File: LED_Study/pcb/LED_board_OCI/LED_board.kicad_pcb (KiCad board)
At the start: 2 copper layers, 25.4 x 25.4 mm, 4 parts

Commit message: new boards
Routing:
- net /Vin: track 10.5 -> 0.00 mm
- net /GND: track 10.5 -> 0.00 mm
- net Net-(D3-Pad1): track 9.07 -> 0.00 mm
- net Net-(D1-Pad1): track 9.07 -> 0.00 mm
- added copper zone on F.Cu, net /GND
- added copper zone on F.Cu, net /Vin
- added copper zone on F.Cu, net Net-(D1-Pad1)
- added copper zone on F.Cu, net Net-(D3-Pad1)
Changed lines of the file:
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@@
   (gr_circle (center 100 100) (end 112.7 100)
     (stroke (width 0.1) (type default)) (fill none) (layer "Edge.Cuts"))
-  (segment (start 94.436 92) (end 92 94.436) (width 1) (layer "F.Cu") (net 1))
-  (segment (start 92 94.436) (end 92 97.25) (width 1) (layer "F.Cu") (net 1))
-  (segment (start 97.25 92) (end 94.436 92) (width 1) (layer "F.Cu") (net 1))
-  (segment (start 92 108) (end 97.25 108) (width 1) (layer "F.Cu") (net 3))
-  (segment (start 92 108) (end 92 102.75) (width 1) (layer "F.Cu") (net 3))
   (via (at 92 108) (size 3) (drill 1.5) (layers "F.Cu" "B.Cu") (free) (net 3))
-  (segment (start 108 92) (end 102.75 92) (width 1) (layer "F.Cu") (net 4))
-  (segment (start 108 92) (end 108 97.25) (width 1) (layer "F.Cu") (net 4))
   (via (at 108 92) (size 3) (drill 1.5) (layers "F.Cu" "B.Cu") (free) (net 4))
-  (segment (start 105.684 108.204) (end 108.12 105.768) (width 1) (layer "F.Cu") (net 6))
-  (segment (start 108.12 105.768) (end 108.12 102.954) (width 1) (layer "F.Cu") (net 6))
-  (segment (start 102.87 108.204) (end 105.684 108.204) (width 1) (layer "F.Cu") (net 6))
+  (zone (net 3) (net_name "/Vin") (layer "F.Cu") (hatch edge 0.5)
+    (priority 1)
+    (connect_pads (clearance 0.5))
+    (min_thickness 0.25) (filled_areas_thickness no)
+    (fill yes (thermal_gap 0.5) (thermal_bridge_width 0.5))
+    (polygon
+      (pts
+        (xy 100 100)
+        (xy 100 114)
+        (xy 86 114)
+        (xy 86 100)
+      )
+    )
+  )
+  (zone (net 4) (net_name "/GND") (layer "F.Cu") (hatch edge 0.5)
+    (priority 3)
+    (connect_pads (clearance 0.5))
+    (min_thickness 0.25) (filled_areas_thickness no)
+    (fill yes (thermal_gap 0.5) (thermal_bridge_width 0.5))
+    (polygon
+      (pts
+        (xy 100 100)
+        (xy 100 86)
+        (xy 113.5 86)
+        (xy 113.5 100)
+      )
+    )
+  )
+  (zone (net 6) (net_name "Net-(D3-Pad1)") (layer "F.Cu") (hatch edge 0.5)
+    (priority 2)
+    (connect_pads (clearance 0.5))
+    (min_thickness 0.25) (filled_areas_thickness no)
+    (fill yes (thermal_gap 0.5) (thermal_bridge_width 0.5))
+    (polygon
+      (pts
+        (xy 100 100)
+        (xy 113.5 100)
+        (xy 113.5 114)
+        (xy 100 114)
+      )
+    )
+  )
+  (zone (net 1) (net_name "Net-(D1-Pad1)") (layer "F.Cu") (hatch edge 0.5)
+    (priority 1)
+    (connect_pads (clearance 0.5))
+    (min_thickness 0.25) (filled_areas_thickness no)
+    (fill yes (thermal_gap 0.5) (thermal_bridge_width 0.5))
+    (polygon
+      (pts
+        (xy 100 100)
+        (xy 100 86)
+        (xy 86 86)
+        (xy 86 100)
+      )
+    )
+  )
 )

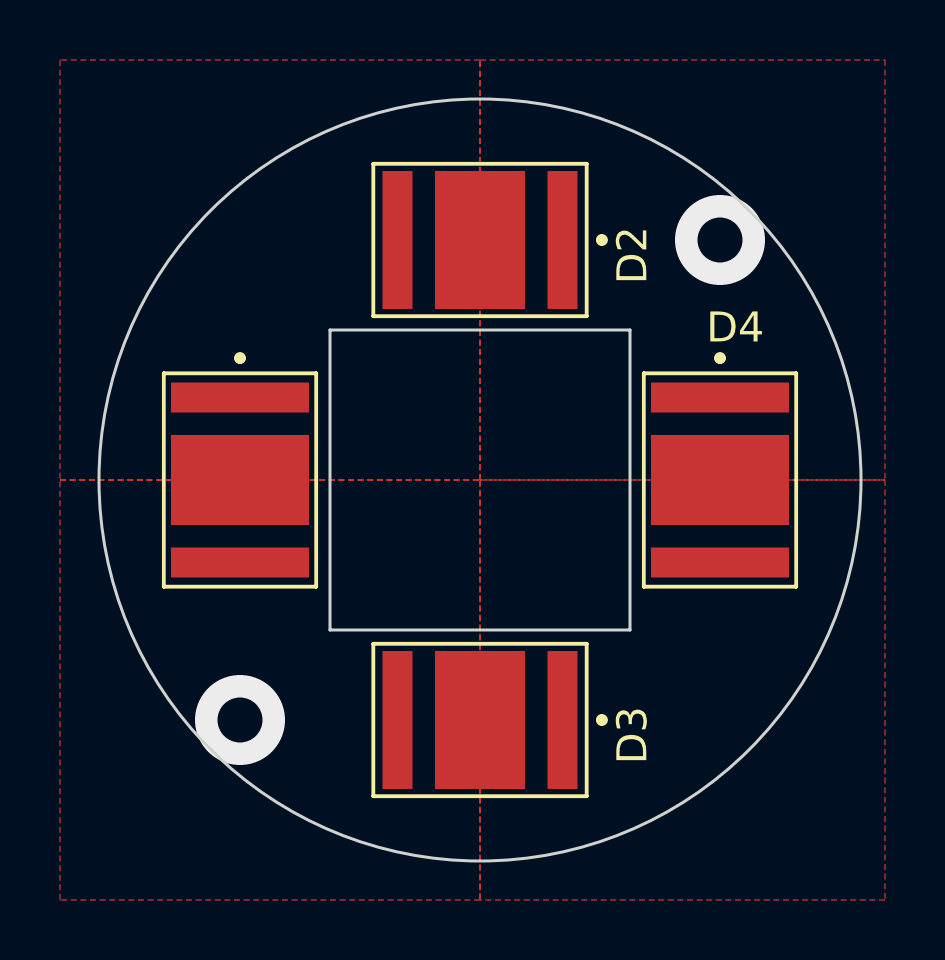
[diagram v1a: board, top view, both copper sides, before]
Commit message: updated boards and ordered from PCBway
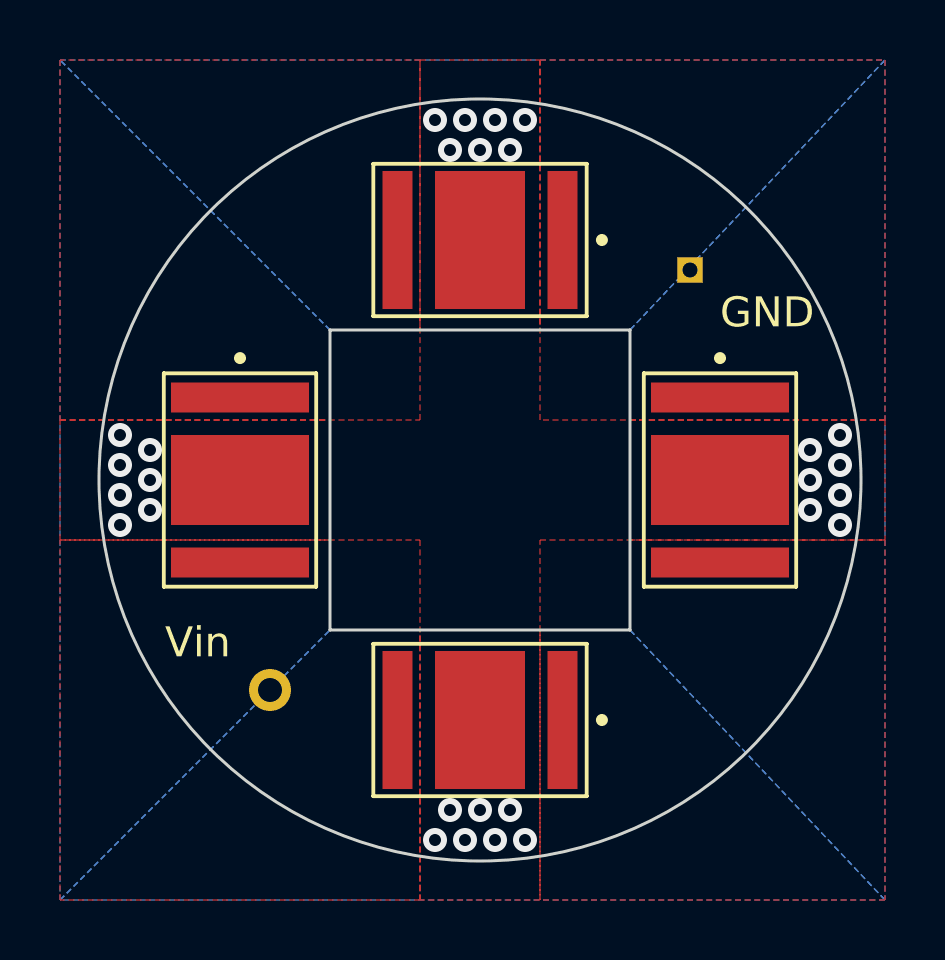
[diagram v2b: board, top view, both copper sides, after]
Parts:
- added J1: Conn_01x01_Pin, Connector_PinHeader_1.00mm:PinHeader_1x01_P1.00mm_Vertical, F.Cu at (93.0, 107.0)
- added J2: Conn_01x01_Pin, Connector_PinHeader_1.00mm:PinHeader_1x01_P1.00mm_Vertical, F.Cu at (107.0, 93.0)
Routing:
- net unconnected-(D4-EXP-Pad3): vias 0 -> 7
- net unconnected-(D3-EXP-Pad3): vias 0 -> 7
- net unconnected-(D2-EXP-Pad3): vias 0 -> 7
- net unconnected-(D1-EXP-Pad3): vias 0 -> 7
- net /Vin: vias 1 -> 0
- net /GND: vias 1 -> 0
- added copper zone on B.Cu, net unconnected-(D1-EXP-Pad3)
- added copper zone on F.Cu, net unconnected-(D1-EXP-Pad3)
- added copper zone on B.Cu, net unconnected-(D2-EXP-Pad3)
- added copper zone on F.Cu, net unconnected-(D2-EXP-Pad3)
- added copper zone on B.Cu, net unconnected-(D3-EXP-Pad3)
- added copper zone on F.Cu, net unconnected-(D3-EXP-Pad3)
- added copper zone on B.Cu, net unconnected-(D4-EXP-Pad3)
- added copper zone on F.Cu, net unconnected-(D4-EXP-Pad3)
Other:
- board text added: "GND"
- board text added: "Vin"
